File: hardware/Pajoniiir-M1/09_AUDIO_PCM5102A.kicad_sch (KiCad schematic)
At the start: 23 parts, among them U5 PCM5102APWR

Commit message: hardware: bind core hierarchical ports to nets
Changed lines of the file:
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@@
     (instances (project "Pajoniiir-M1" (path "/2c8dd352-b7b8-4d9e-8f93-5dd43be2a100/31000009-6b2a-4a3a-8c91-000000000009" (reference "#PWR0905") (unit 1))))
   )
-  (hierarchical_label "3V3_AUDIO" (shape input) (at 45.085 40.005 0) (effects (font (size 1.27 1.27))))
+  (hierarchical_label "3V3_AUDIO" (shape input) (at 55.245 40.005 0) (effects (font (size 1.27 1.27))))
   (symbol
     (lib_id "Device:C") (at 55.245 43.815 0) (unit 1)
@@
     (instances (project "Pajoniiir-M1" (path "/2c8dd352-b7b8-4d9e-8f93-5dd43be2a100/31000009-6b2a-4a3a-8c91-000000000009" (reference "C_AUDIO_BRANCH") (unit 1))))
   )
-  (label "3V3_AUDIO" (at 55.245 40.005 0) (effects (font (size 1.27 1.27))))
   (symbol
     (lib_id "power:GND") (at 55.245 47.625 0) (unit 1)

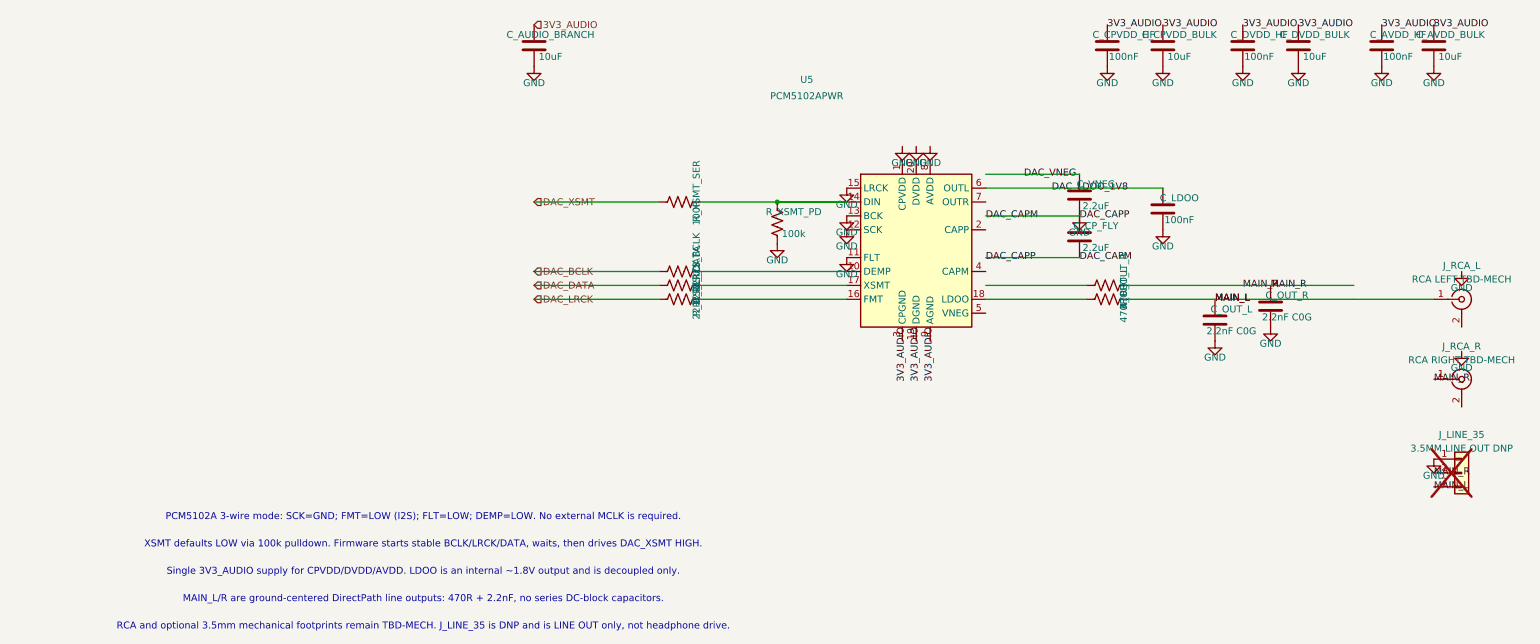
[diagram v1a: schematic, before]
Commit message: hardware: correct PCM5102A pin and audio net mapping
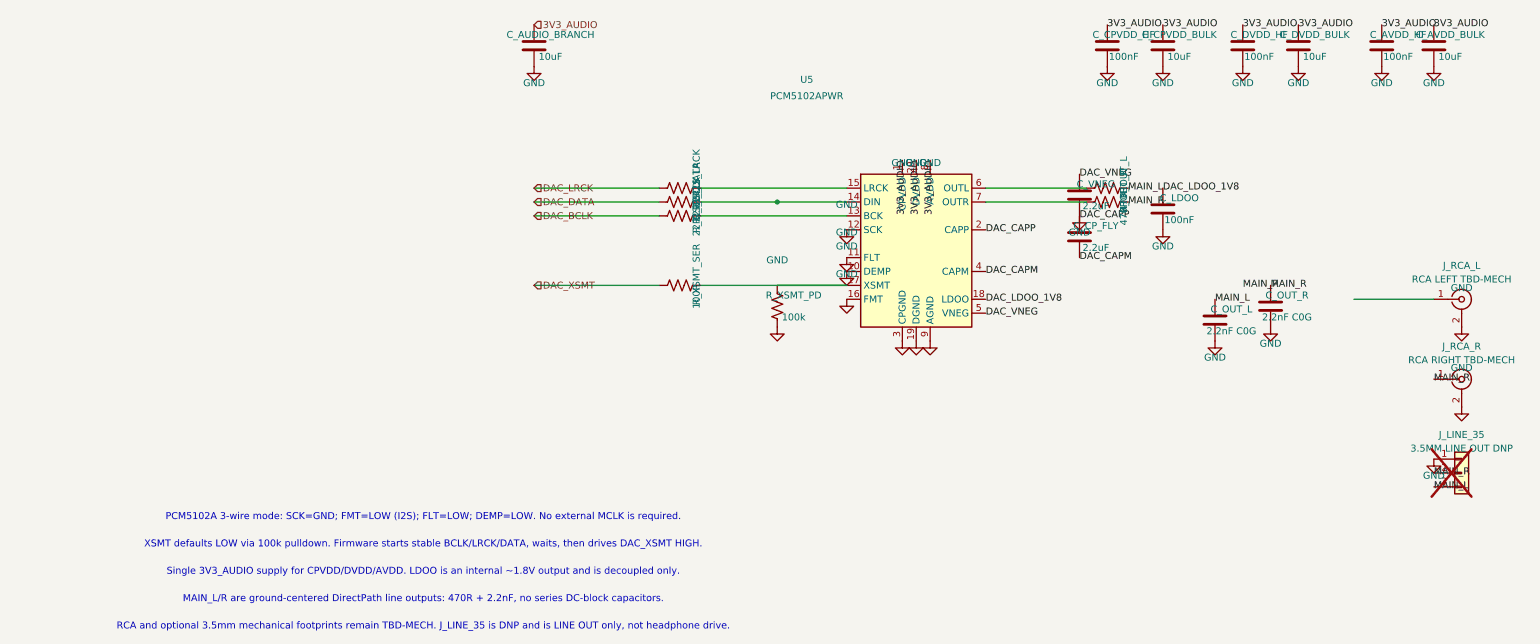
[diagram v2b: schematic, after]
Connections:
- net 3V3_AUDIO: now also U5.1 (CPVDD), U5.20 (DVDD), U5.8 (AVDD)
- net DAC_LDOO_1V8: now also U5.18 (LDOO); no longer U5.6 (OUTL)
- net DAC_VNEG: now also U5.5 (VNEG)
- net GND: now also J_RCA_L.2 (Ext), J_RCA_R.2 (Ext), U5.10 (DEMP), U5.16 (FMT), U5.19 (DGND), U5.2 (CAPP), U5.3 (CPGND), U5.9 (AGND); no longer C_CP_FLY.2, U5.13 (BCK), U5.15 (LRCK)
- net MAIN_L: no longer J_RCA_L.1 (In)
- net at R_I2S_BCLK.2: now also U5.13 (BCK); no longer U5.10 (DEMP)
- net at R_XSMT_PD.1, R_XSMT_SER.2: now also U5.17 (XSMT); no longer U5.14 (DIN)
- net at R_I2S_LRCK.2: now also U5.15 (LRCK); no longer U5.16 (FMT)
- net at R_I2S_DATA.2: now also U5.14 (DIN); no longer U5.17 (XSMT)
- net at R_OUT_L.1: now also U5.6 (OUTL); no longer U5.18 (LDOO)
- net DAC_CAPM: now reaches U5.4 (CAPM)
- net DAC_CAPM: now also C_CP_FLY.2
- net at U5.7 (OUTR): now also R_OUT_R.1
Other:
- moved on the sheet: R_I2S_BCLK, R_I2S_DATA, R_I2S_LRCK, R_OUT_L, R_OUT_R, R_XSMT_PD, R_XSMT_SER

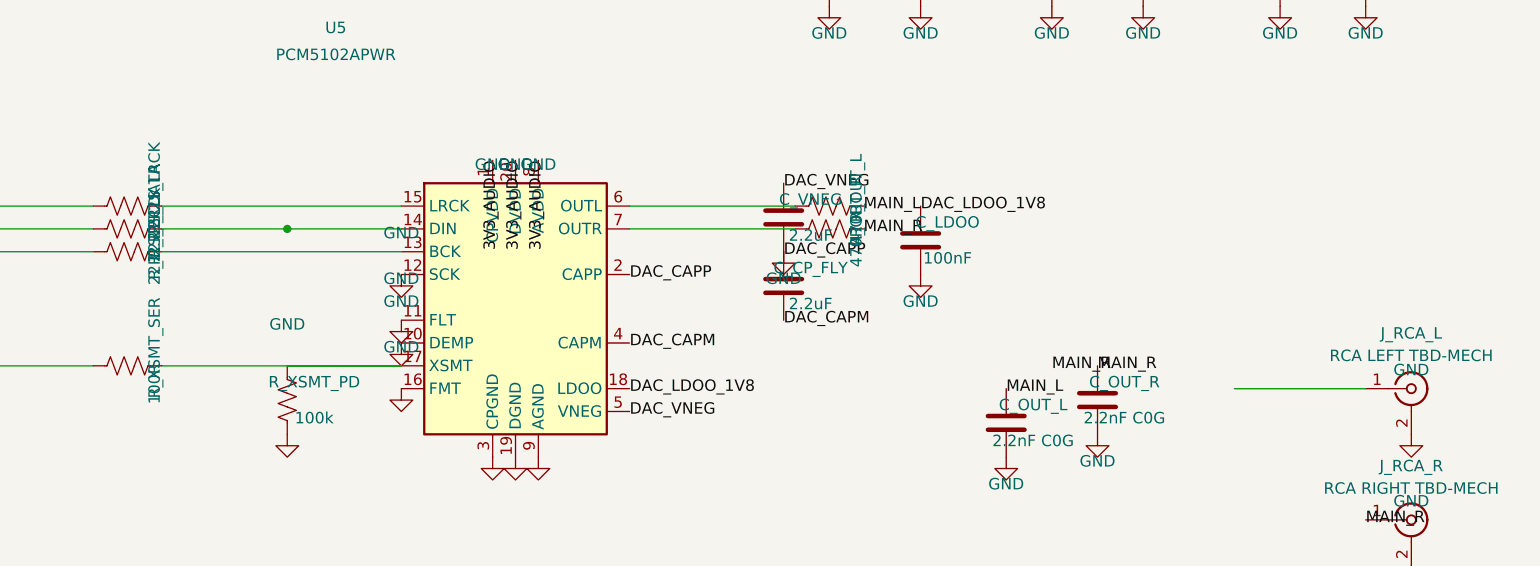
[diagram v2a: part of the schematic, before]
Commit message: hardware: close peripheral endpoint and net-alias gaps
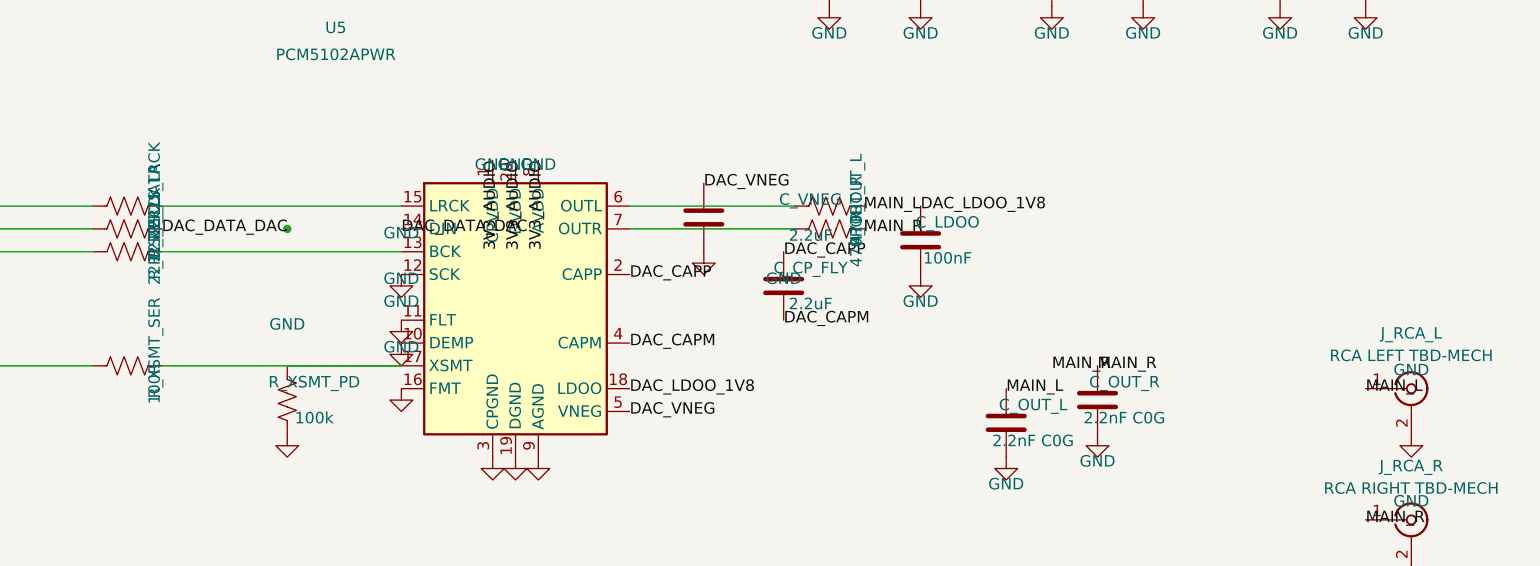
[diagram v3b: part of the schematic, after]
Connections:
- net GND: no longer C_CP_FLY.1, U5.2 (CAPP)
- net MAIN_L: now also J_RCA_L.1 (In)
- net DAC_DATA_DAC: now reaches R_I2S_DATA.2, U5.14 (DIN)
- new net DAC_CAPP: C_CP_FLY.1, U5.2 (CAPP)
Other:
- moved on the sheet: C_VNEG
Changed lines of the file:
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@@
     (comment 2 "Cue/PFL remains USB1 UAC ch3/ch4 to DDJ-FLX4")
   )
+  (label "DAC_DATA_DAC" (at 85.725 72.39 0) (effects (font (size 1.27 1.27))))
+  (label "DAC_DATA_DAC" (at 112.395 72.39 0) (effects (font (size 1.27 1.27))))
+  (label "MAIN_L" (at 219.71 90.17 0) (effects (font (size 1.27 1.27))))
   (label "DAC_VNEG" (at 137.795 92.71 0) (effects (font (size 1.27 1.27))))
   (label "DAC_LDOO_1V8" (at 137.795 90.17 0) (effects (font (size 1.27 1.27))))
@@
   )
   (wire (pts (xy 55.245 72.39) (xy 78.105 72.39)) (stroke (width 0) (type default)))
-  (wire (pts (xy 85.725 72.39) (xy 112.395 72.39)) (stroke (width 0) (type default)))
   (hierarchical_label "DAC_BCLK" (shape input) (at 55.245 74.93 0) (effects (font (size 1.27 1.27))))
   (symbol
@@
   (label "DAC_CAPM" (at 137.795 85.09 0) (effects (font (size 1.27 1.27))))
   (symbol
-    (lib_id "Device:C") (at 154.94 71.12 0) (unit 1)
+    (lib_id "Device:C") (at 146.05 71.12 0) (unit 1)
     (exclude_from_sim no) (in_bom yes) (on_board yes) (dnp no)
     (property "Reference" "C_VNEG" (at 157.94 69.12 0) (effects (font (size 1.27 1.27))))
@@
     (instances (project "Pajoniiir-M1" (path "/2c8dd352-b7b8-4d9e-8f93-5dd43be2a100/31000009-6b2a-4a3a-8c91-000000000009" (reference "C_VNEG") (unit 1))))
   )
-  (label "DAC_VNEG" (at 154.94 67.31 0) (effects (font (size 1.27 1.27))))
-  (symbol
-    (lib_id "power:GND") (at 154.94 74.93 0) (unit 1)
+  (label "DAC_VNEG" (at 146.05 67.31 0) (effects (font (size 1.27 1.27))))
+  (symbol
+    (lib_id "power:GND") (at 146.05 74.93 0) (unit 1)
     (exclude_from_sim no) (in_bom yes) (on_board yes) (dnp no)
     (property "Reference" "#PWR0910" (at 154.94 80.93 0) (effects (font (size 1.27 1.27)) (hide yes)))
@@
     (instances (project "Pajoniiir-M1" (path "/2c8dd352-b7b8-4d9e-8f93-5dd43be2a100/31000009-6b2a-4a3a-8c91-000000000009" (reference "J_RCA_L") (unit 1))))
   )
-  (wire (pts (xy 205.105 90.17) (xy 219.71 90.17)) (stroke (width 0) (type default)))
   (symbol
     (lib_id "power:GND") (at 224.79 95.25 0) (unit 1)

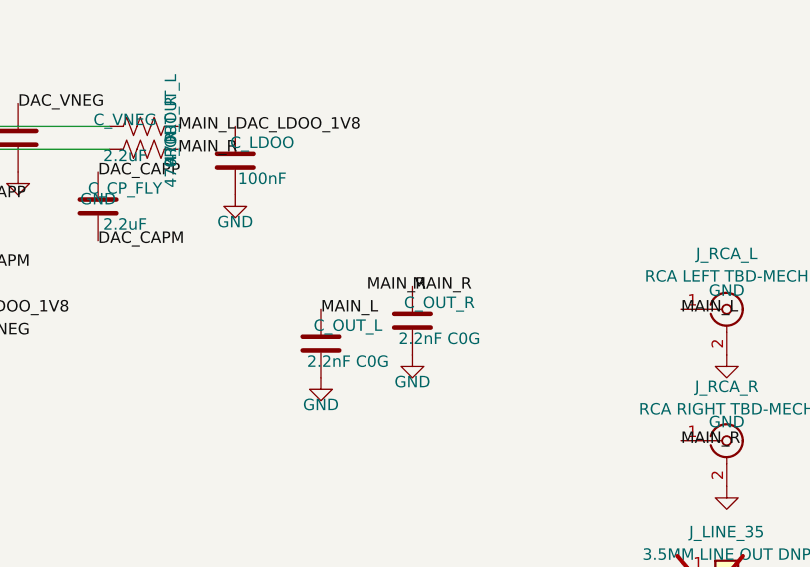
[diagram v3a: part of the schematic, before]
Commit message: hardware: normalize endpoint nets and fix microSD input rail
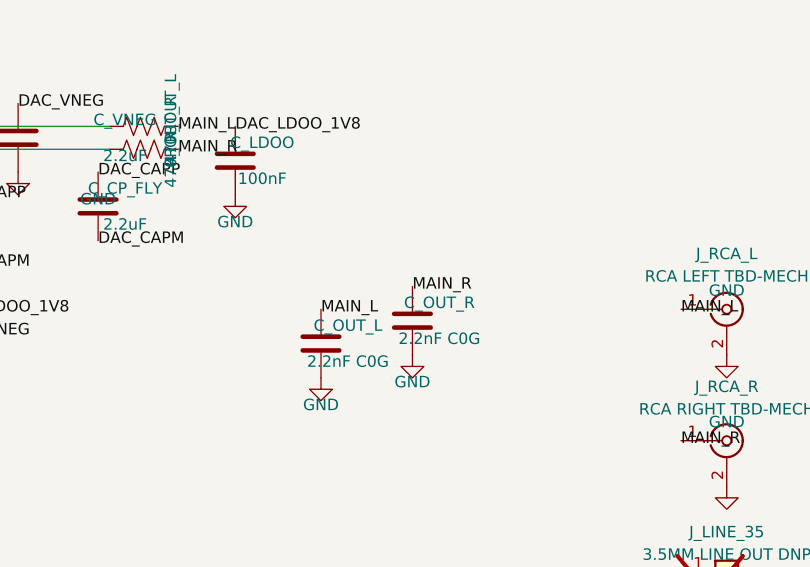
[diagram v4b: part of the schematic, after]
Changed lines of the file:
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@@
   )
   (wire (pts (xy 137.795 72.39) (xy 156.21 72.39)) (stroke (width 0) (type default)))
-  (label "MAIN_R" (at 184.785 87.63 0) (effects (font (size 1.27 1.27))))
   (symbol
     (lib_id "Device:C") (at 189.865 91.44 0) (unit 1)

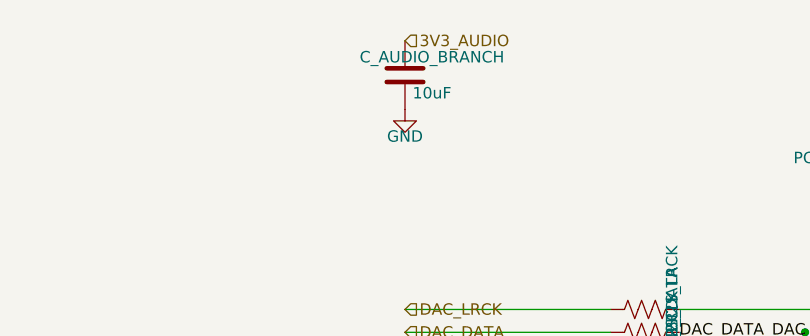
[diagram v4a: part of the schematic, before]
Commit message: hardware: declare verified rail power sources for ERC
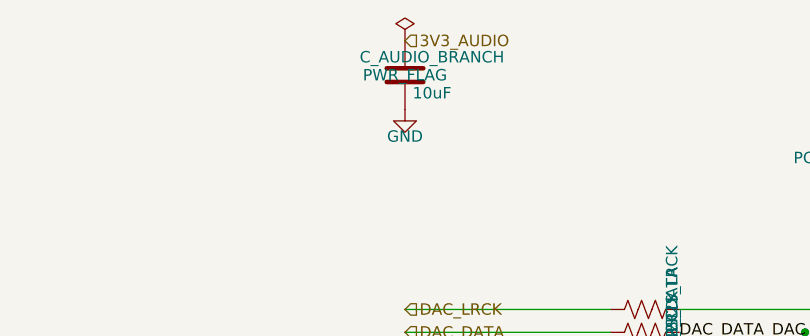
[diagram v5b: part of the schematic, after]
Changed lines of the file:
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@@
   (text "MAIN_L/R are ground-centered DirectPath line outputs: 470R + 2.2nF, no series DC-block capacitors." (exclude_from_sim no) (at 35 145 0) (effects (font (size 1.27 1.27))))
   (text "RCA and optional 3.5mm mechanical footprints remain TBD-MECH. J_LINE_35 is DNP and is LINE OUT only, not headphone drive." (exclude_from_sim no) (at 35 150 0) (effects (font (size 1.27 1.27))))
+  (symbol
+    (lib_id "power:PWR_FLAG")
+    (at 55.245 40.005 0)
+    (unit 1)
+    (exclude_from_sim no)
+    (in_bom yes)
+    (on_board yes)
+    (dnp no)
+    (property "Reference" "#FLG0901" (at 55.245 41.910000000000004 0) (effects (font (size 1.27 1.27)) (hide yes)))
+    (property "Value" "PWR_FLAG" (at 55.245 43.815000000000005 0) (effects (font (size 1.27 1.27))))
+    (property "Footprint" "" (at 55.245 40.005 0) (effects (font (size 1.27 1.27)) (hide yes)))
+    (property "Datasheet" "~" (at 55.245 40.005 0) (effects (font (size 1.27 1.27)) (hide yes)))
+    (property "Description" "Special symbol for telling ERC where power comes from" (at 55.245 40.005 0) (effects (font (size 1.27 1.27)) (hide yes)))
+    (pin "1")
+    (instances (project "Pajoniiir-M1" (path "/2c8dd352-b7b8-4d9e-8f93-5dd43be2a100/31000009-6b2a-4a3a-8c91-000000000009" (reference "#FLG0901") (unit 1))))
+  )
   (sheet_instances (path "/" (page "10")))
   (embedded_fonts no)
